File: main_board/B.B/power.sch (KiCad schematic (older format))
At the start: 36 parts, among them Q1 CJ3134K, Q2 CJ3134K, U62 AOZ1280, U63 FP6296

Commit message: nabijecka
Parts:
- removed C100: 47nf, Capacitor_SMD:C_0603_1608Metric, symbol Device:C
- removed C101: 10pf, Capacitor_SMD:C_0402_1005Metric, symbol Device:C
- removed C91, C95: 22uf, Capacitor_SMD:C_0805_2012Metric, symbol Device:C
- removed C96: 2.2uf, Capacitor_SMD:C_0805_2012Metric, symbol Device:C
- removed C97: 100nf, Capacitor_SMD:C_0402_1005Metric, symbol Device:C
- removed C98: 1nf, Capacitor_SMD:C_0402_1005Metric, symbol Device:C
- removed C99: 1uf, Capacitor_SMD:C_0402_1005Metric, symbol Device:C
- removed D2: SS54, BB:DO-214AC, symbol Device:D_Schottky
- removed L2: 3.3uH, BB:SMD-PIND-12.8x13.5x5_2.0x5.0, symbol Device:L
- removed Q2: CJ3134K, Package_TO_SOT_SMD:SOT-23, symbol Transistor_FET:2N7002
- removed R13: 10, Resistor_SMD:R_0402_1005Metric, symbol Device:R
- removed R15: 1.5, Resistor_SMD:R_0402_1005Metric, symbol Device:R
- removed R16: 24k, Resistor_SMD:R_0402_1005Metric, symbol Device:R
- removed R17: 100k, Resistor_SMD:R_0402_1005Metric, symbol Device:R
- removed R19: 8,2k, Resistor_SMD:R_0402_1005Metric, symbol Device:R
- removed U63: FP6296, BB:SOP-8+1_3.76x4.96mm_P1.27mm, symbol B.B-rescue:FP6296
- added C61: 1uf, Capacitor_SMD:C_0402_1005Metric, symbol Device:C
- added C62: 2.2uf, Capacitor_SMD:C_0805_2012Metric, symbol Device:C
- added C?: 22uf, Capacitor_SMD:C_0805_2012Metric, symbol Device:C
- added L?: 2.2uH, BB:MWSA0603_6.6x7.1x3.0, symbol Device:L
- added Q?: 2N7002, Package_TO_SOT_SMD:SOT-23, symbol Transistor_FET:2N7002
- added R7, R8: 1M, Resistor_SMD:R_0402_1005Metric, symbol Device:R
- added R?: 7.5k, Resistor_SMD:R_0402_1005Metric, symbol Device:R
- added R?: 56k, Resistor_SMD:R_0402_1005Metric, symbol Device:R
- added SW3: SW_DIP_x01, Button_Switch_SMD:SW_Push_1P1T_NO_CK_KSC6xxJ, symbol Switch:SW_DIP_x01
- added U?: FP6276, Package_SO:SOP-8_3.76x4.96mm_P1.27mm, symbol B.B-rescue:FP6276
- L1: footprint BB:SMD-PIND-10.5x11.5x4_2.5x3.0 -> BB:MWSA0603_6.6x7.1x3.0; LCSC C149550 -> C112126
- Q1: value CJ3134K -> 2N7002; LCSC C110100 -> C8545
- R14: value 75k -> 56k; LCSC C25798 -> C25796
- gave numbers to parts that had none: 2
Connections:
- wire segments 77 -> 71

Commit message: 18650
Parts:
- removed C86: 2.2uf, Capacitor_SMD:C_0805_2012Metric, symbol Device:C
- gave numbers to parts that had none: 6
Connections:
- wire segments 71 -> 69

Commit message: polifuse
-filtr k prijmaci IR
-merwni bterky -> za zapinani
-odstraneni odpojovani nabijecky + oprava napajeciho prouhu
-odstraneni prevodniku napeti k WS2812
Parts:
- added R3: 1M, Resistor_SMD:R_0402_1005Metric, symbol Device:R
- added R4: 300k, Capacitor_SMD:C_0402_1005Metric, symbol Device:R
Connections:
- net labels added: VCC-OUT, baterimetr
- wire segments 69 -> 74
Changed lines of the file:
@@
 Connection ~ 4950 2525
 Connection ~ 4625 2525
+$Comp
+L Device:R R?
+U 1 1 5FBC25E2
+P 3975 4750
+AR Path="/5FBC25E2" Ref="R?"  Part="1"
+AR Path="/5FA4C94D/5FBC25E2" Ref="R4"  Part="1"
+F 0 "R4" H 4045 4796 50  0000 L CNN
+F 1 "300k" H 4045 4705 50  0000 L CNN
+F 2 "Capacitor_SMD:C_0402_1005Metric" V 3905 4750 50  0001 C CNN
+F 3 "~" H 3975 4750 50  0001 C CNN
+F 4 "C25774" H 3975 4750 50  0001 C CNN "LCSC"
+	1    3975 4750
+	1    0    0    -1
+$EndComp
+$Comp
+L B.B-eagle-import:GND #GND?
+U 1 1 5FBC25E8
+P 3975 5000
+AR Path="/5FBC25E8" Ref="#GND?"  Part="1"
+AR Path="/5FA4C94D/5FBC25E8" Ref="#GND0158"  Part="1"
+F 0 "#GND0158" H 3975 5000 50  0001 C CNN
+F 1 "GND" H 3975 4920 59  0000 C CNN
+F 2 "" H 3975 5000 50  0001 C CNN
+F 3 "" H 3975 5000 50  0001 C CNN
+	1    3975 5000
+	1    0    0    -1
+$EndComp
+Wire Wire Line
+	3825 4600 3975 4600
+$Comp
+L Device:R R?
+U 1 1 5FBC25F0
+P 3975 4450
+AR Path="/5F77B818/5FBC25F0" Ref="R?"  Part="1"
+AR Path="/5FBC25F0" Ref="R?"  Part="1"
+AR Path="/5FA4C94D/5FBC25F0" Ref="R3"  Part="1"
+F 0 "R3" H 4045 4496 50  0000 L CNN
+F 1 "1M" H 4045 4405 50  0000 L CNN
+F 2 "Resistor_SMD:R_0402_1005Metric" V 3905 4450 50  0001 C CNN
+F 3 "~" H 3975 4450 50  0001 C CNN
+F 4 "C26083" H 3975 4450 50  0001 C CNN "LCSC"
+	1    3975 4450
+	1    0    0    -1
+$EndComp
+Connection ~ 3975 4600
+Wire Wire Line
+	3975 4300 3975 4275
+Wire Wire Line
+	3975 4275 4625 4275
+Text HLabel 3825 4600 0    50   Input ~ 0
+baterimetr
+Text HLabel 4675 2425 2    50   Input ~ 0
+VCC-OUT
+Wire Wire Line
+	4675 2425 4625 2425
+Wire Wire Line
+	4625 2425 4625 2525
 $EndSCHEMATC

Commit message: popisky
-popisky
-poladeni uddeleni enkoderu
-poladeni nayvu drah
-priopjeni gnd USB
-poligon V5 na led-desce do spodni vrstvu
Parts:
- C61, C62, C75, C85, C87, C88, C89, C90, C92, C93: symbol Device:C -> B.B-rescue:C-Device
- D1: symbol Device:D_Schottky -> B.B-rescue:D_Schottky-Device
- L1, L2: symbol Device:L -> B.B-rescue:L-Device
- Q1, Q2: symbol Transistor_FET:2N7002 -> B.B-rescue:2N7002-Transistor_FET
- R10, R11, R12, R13, R14, R15, R18, R3, R4, R6, R7, R8: symbol Device:R -> B.B-rescue:R-Device
- SW3: symbol Switch:SW_DIP_x01 -> B.B-rescue:SW_DIP_x01-Switch
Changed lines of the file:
@@
 EESchema Schematic File Version 4
-LIBS:B.B-cache
-EELAYER 29 0
+EELAYER 30 0
 EELAYER END
 $Descr A4 11693 8268
@@
 $EndComp
 $Comp
-L Device:C C88
+L B.B-rescue:C-Device C88
 U 1 1 5FA5C393
 P 7725 2825
@@
 $EndComp
 $Comp
-L Device:C C87
+L B.B-rescue:C-Device C87
 U 1 1 5FA66714
 P 4950 2725
@@
 $EndComp
 $Comp
-L Device:R R10
+L B.B-rescue:R-Device R10
 U 1 1 5FA82308
 P 5575 2675
@@
 	5275 2525 5925 2525
 $Comp
-L Device:R R11
+L B.B-rescue:R-Device R11
 U 1 1 5FAAA54F
 P 6925 2725
@@
 	7225 2775 7225 2625
 $Comp
-L Device:R R12
+L B.B-rescue:R-Device R12
 U 1 1 5FAAA559
 P 6625 2925
@@
 	7225 2625 7275 2625
 $Comp
-L Device:C C85
+L B.B-rescue:C-Device C85
 U 1 1 5FACBCDA
 P 6775 2525
@@
 	7225 2525 7225 2625
 $Comp
-L Device:D_Schottky D1
+L B.B-rescue:D_Schottky-Device D1
 U 1 1 5FAEBDB1
 P 7225 2925
@@
 Connection ~ 7625 2625
 $Comp
-L Device:R R14
+L B.B-rescue:R-Device R14
 U 1 1 5FA6804A
 P 6775 4475
@@
 $EndComp
 $Comp
-L Device:C C92
+L B.B-rescue:C-Device C92
 U 1 1 5FA68060
 P 7125 4475
@@
 $EndComp
 $Comp
-L Device:C C93
+L B.B-rescue:C-Device C93
 U 1 1 5FA68067
 P 7550 4475
@@
 $EndComp
 $Comp
-L Device:C C90
+L B.B-rescue:C-Device C90
 U 1 1 5FCAA96B
 P 4625 4475
@@
 	5625 4275 5475 4275
 $Comp
-L Transistor_FET:2N7002 Q?
+L B.B-rescue:2N7002-Transistor_FET Q?
 U 1 1 5FA8B0DC
 P 3275 3025
@@
 $EndComp
 $Comp
-L Device:R R6
+L B.B-rescue:R-Device R6
 U 1 1 602F171D
 P 3175 2825
@@
 pull-up to 3V3 in ESP32
 $Comp
-L Device:L L1
+L B.B-rescue:L-Device L1
 U 1 1 5FBDFC00
 P 7425 2625
@@
 SHUTDOWN_3V3-5V
 $Comp
-L Device:C C62
+L B.B-rescue:C-Device C62
 U 1 1 5FC4D1AC
 P 2925 3225
@@
 $EndComp
 $Comp
-L Device:R R?
+L B.B-rescue:R-Device R?
 U 1 1 5FC4F9B1
 P 2625 3225
@@
 	2625 3075 2625 3025
 $Comp
-L Switch:SW_DIP_x01 SW?
+L B.B-rescue:SW_DIP_x01-Switch SW?
 U 1 1 5FC5B229
 P 4275 3500
@@
 $EndComp
 $Comp
-L Device:C C61
+L B.B-rescue:C-Device C61
 U 1 1 5FC601F5
 P 4050 2825
@@
 $EndComp
 $Comp
-L Device:R R?
+L B.B-rescue:R-Device R?
 U 1 1 5FC61828
 P 4050 3050
@@
 	5550 4800 5550 4675
 $Comp
-L Transistor_FET:2N7002 Q?
+L B.B-rescue:2N7002-Transistor_FET Q?
 U 1 1 5FBA36C7
 P 5450 5000
@@
 $EndComp
 $Comp
-L Device:R R18
+L B.B-rescue:R-Device R18
 U 1 1 5FCDFEDA
 P 5325 4675
@@
 	7550 4275 7975 4275
 $Comp
-L Device:R R13
+L B.B-rescue:R-Device R13
 U 1 1 5FBBDF29
 P 6775 4775
@@
 Connection ~ 6775 4625
 $Comp
-L Device:C C75
+L B.B-rescue:C-Device C75
 U 1 1 5FBDCDD3
 P 7975 4475
@@
 	7975 4275 8325 4275
 $Comp
-L Device:L L2
+L B.B-rescue:L-Device L2
 U 1 1 5FBEEA97
 P 5325 4275
@@
 $EndComp
 $Comp
-L Device:R R15
+L B.B-rescue:R-Device R15
 U 1 1 5FBF0991
 P 6375 4875
@@
 $EndComp
 $Comp
-L Device:C C89
+L B.B-rescue:C-Device C89
 U 1 1 5FA5C39A
 P 8125 2825
@@
 Connection ~ 4625 2525
 $Comp
-L Device:R R?
+L B.B-rescue:R-Device R?
 U 1 1 5FBC25E2
 P 3975 4750
@@
 	3825 4600 3975 4600
 $Comp
-L Device:R R?
+L B.B-rescue:R-Device R?
 U 1 1 5FBC25F0
 P 3975 4450

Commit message: LDC footprint
prodlouzeni pedu pro usnadneni rucniho osazovani
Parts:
- C61, C62, C75, C85, C87, C88, C89, C90, C92, C93: symbol B.B-rescue:C-Device -> B.B-rescue:C-Device-B.B-rescue
- D1: symbol B.B-rescue:D_Schottky-Device -> B.B-rescue:D_Schottky-Device-B.B-rescue
- L1, L2: symbol B.B-rescue:L-Device -> B.B-rescue:L-Device-B.B-rescue
- Q1, Q2: symbol B.B-rescue:2N7002-Transistor_FET -> B.B-rescue:2N7002-Transistor_FET-B.B-rescue
- Q5: symbol B.B-rescue:Q_PMOS_DSG -> B.B-rescue:Q_PMOS_DSG-B.B-rescue
- R10, R11, R12, R13, R14, R15, R18, R3, R4, R6, R7, R8: symbol B.B-rescue:R-Device -> B.B-rescue:R-Device-B.B-rescue
- SW3: symbol B.B-rescue:SW_DIP_x01-Switch -> B.B-rescue:SW_DIP_x01-Switch-B.B-rescue
- U62: symbol B.B-rescue:AOZ1280 -> B.B-rescue:AOZ1280-B.B-rescue
- U63: symbol B.B-rescue:FP6276 -> B.B-rescue:FP6276-B.B-rescue
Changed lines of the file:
@@
 VCC
 $Comp
-L B.B-rescue:AOZ1280 U62
+L B.B-rescue:AOZ1280-B.B-rescue U62
 U 1 1 5FA53B6D
 P 6225 2525
@@
 $EndComp
 $Comp
-L B.B-rescue:C-Device C88
+L B.B-rescue:C-Device-B.B-rescue C88
 U 1 1 5FA5C393
 P 7725 2825
@@
 	7725 2675 7725 2625
 $Comp
-L B.B-eagle-import:GND #GND088
+L B.B-rescue:GND-B.B-eagle-import #GND088
 U 1 1 5FA5C3A3
 P 7725 3075
@@
 $EndComp
 $Comp
-L B.B-rescue:C-Device C87
+L B.B-rescue:C-Device-B.B-rescue C87
 U 1 1 5FA66714
 P 4950 2725
@@
 $EndComp
 $Comp
-L B.B-eagle-import:GND #GND086
+L B.B-rescue:GND-B.B-eagle-import #GND086
 U 1 1 5FA6671A
 P 4950 2975
@@
 	6525 2625 7225 2625
 $Comp
-L B.B-eagle-import:GND #GND087
+L B.B-rescue:GND-B.B-eagle-import #GND087
 U 1 1 5FA8018B
 P 6225 2975
@@
 $EndComp
 $Comp
-L B.B-rescue:R-Device R10
+L B.B-rescue:R-Device-B.B-rescue R10
 U 1 1 5FA82308
 P 5575 2675
@@
 	5275 2675 5275 2525
 $Comp
-L B.B-eagle-import:GND #GND?
+L B.B-rescue:GND-B.B-eagle-import #GND?
 U 1 1 5FA8231A
 P 3375 3325
@@
 	5275 2525 5925 2525
 $Comp
-L B.B-rescue:R-Device R11
+L B.B-rescue:R-Device-B.B-rescue R11
 U 1 1 5FAAA54F
 P 6925 2725
@@
 	7225 2775 7225 2625
 $Comp
-L B.B-rescue:R-Device R12
+L B.B-rescue:R-Device-B.B-rescue R12
 U 1 1 5FAAA559
 P 6625 2925
@@
 	6625 2725 6525 2725
 $Comp
-L B.B-eagle-import:GND #GND090
+L B.B-rescue:GND-B.B-eagle-import #GND090
 U 1 1 5FAAA562
 P 6625 3175
@@
 	7225 2625 7275 2625
 $Comp
-L B.B-rescue:C-Device C85
+L B.B-rescue:C-Device-B.B-rescue C85
 U 1 1 5FACBCDA
 P 6775 2525
@@
 	7225 2525 7225 2625
 $Comp
-L B.B-rescue:D_Schottky-Device D1
+L B.B-rescue:D_Schottky-Device-B.B-rescue D1
 U 1 1 5FAEBDB1
 P 7225 2925
@@
 $EndComp
 $Comp
-L B.B-eagle-import:GND #GND091
+L B.B-rescue:GND-B.B-eagle-import #GND091
 U 1 1 5FAECA44
 P 7225 3175
@@
 Connection ~ 7625 2625
 $Comp
-L B.B-rescue:R-Device R14
+L B.B-rescue:R-Device-B.B-rescue R14
 U 1 1 5FA6804A
 P 6775 4475
@@
 $EndComp
 $Comp
-L B.B-eagle-import:GND #GND0102
+L B.B-rescue:GND-B.B-eagle-import #GND0102
 U 1 1 5FA68059
 P 6775 5025
@@
 $EndComp
 $Comp
-L B.B-rescue:C-Device C92
+L B.B-rescue:C-Device-B.B-rescue C92
 U 1 1 5FA68060
 P 7125 4475
@@
 $EndComp
 $Comp
-L B.B-rescue:C-Device C93
+L B.B-rescue:C-Device-B.B-rescue C93
 U 1 1 5FA68067
 P 7550 4475
@@
 	7125 4275 7550 4275
 $Comp
-L B.B-eagle-import:GND #GND096
+L B.B-rescue:GND-B.B-eagle-import #GND096
 U 1 1 5FA68099
 P 7125 4725
@@
 $EndComp
 $Comp
-L B.B-eagle-import:GND #GND097
+L B.B-rescue:GND-B.B-eagle-import #GND097
 U 1 1 5FA6809F
 P 7550 4725
@@
 	6775 4275 7125 4275
 $Comp
-L B.B-eagle-import:GND #GND0106
+L B.B-rescue:GND-B.B-eagle-import #GND0106
 U 1 1 5FBAAAC6
 P 5975 4925
@@
 $EndComp
 $Comp
-L B.B-rescue:C-Device C90
+L B.B-rescue:C-Device-B.B-rescue C90
 U 1 1 5FCAA96B
 P 4625 4475
@@
 	4625 4325 4625 4275
 $Comp
-L B.B-eagle-import:GND #GND094
+L B.B-rescue:GND-B.B-eagle-import #GND094
 U 1 1 5FCAA97A
 P 4625 4725
@@
 	5625 4275 5475 4275
 $Comp
-L B.B-rescue:2N7002-Transistor_FET Q?
+L B.B-rescue:2N7002-Transistor_FET-B.B-rescue Q?
 U 1 1 5FA8B0DC
 P 3275 3025
@@
 	5725 2675 5925 2675
 $Comp
-L B.B-rescue:Q_PMOS_DSG Q?
+L B.B-rescue:Q_PMOS_DSG-B.B-rescue Q?
 U 1 1 602B4407
 P 3375 2625
@@
 $EndComp
 $Comp
-L B.B-rescue:R-Device R6
+L B.B-rescue:R-Device-B.B-rescue R6
 U 1 1 602F171D
 P 3175 2825
@@
 pull-up to 3V3 in ESP32
 $Comp
-L B.B-rescue:L-Device L1
+L B.B-rescue:L-Device-B.B-rescue L1
 U 1 1 5FBDFC00
 P 7425 2625
@@
 SHUTDOWN_3V3-5V
 $Comp
-L B.B-rescue:C-Device C62
+L B.B-rescue:C-Device-B.B-rescue C62
 U 1 1 5FC4D1AC
 P 2925 3225
@@
 	2925 3025 2925 3075
 $Comp
-L B.B-eagle-import:GND #GND0131
+L B.B-rescue:GND-B.B-eagle-import #GND0131
 U 1 1 5FC4D1B3
 P 2925 3475
@@
 $EndComp
 $Comp
-L B.B-rescue:R-Device R?
+L B.B-rescue:R-Device-B.B-rescue R?
 U 1 1 5FC4F9B1
 P 2625 3225
@@
 $EndComp
 $Comp
-L B.B-eagle-import:GND #GND0135
+L B.B-rescue:GND-B.B-eagle-import #GND0135
 U 1 1 5FC515F0
 P 2625 3475
@@
 	2625 3075 2625 3025
 $Comp
-L B.B-rescue:SW_DIP_x01-Switch SW?
+L B.B-rescue:SW_DIP_x01-Switch-B.B-rescue SW?
 U 1 1 5FC5B229
 P 4275 3500
@@
 $EndComp
 $Comp
-L B.B-rescue:C-Device C61
+L B.B-rescue:C-Device-B.B-rescue C61
 U 1 1 5FC601F5
 P 4050 2825
@@
 $EndComp
 $Comp
-L B.B-rescue:R-Device R?
+L B.B-rescue:R-Device-B.B-rescue R?
 U 1 1 5FC61828
 P 4050 3050
@@
 	4275 3050 4275 3200
 $Comp
-L B.B-eagle-import:GND #GND0136
+L B.B-rescue:GND-B.B-eagle-import #GND0136
 U 1 1 5FC7161E
 P 4275 3900
@@
 $EndComp
 $Comp
-L B.B-rescue:FP6276 U63
+L B.B-rescue:FP6276-B.B-rescue U63
 U 1 1 5FB47E0B
 P 5975 4275
@@
 	6375 4675 6325 4675
 $Comp
-L B.B-eagle-import:GND #GND0101
+L B.B-rescue:GND-B.B-eagle-import #GND0101
 U 1 1 5FB82735
 P 6375 5125
@@
 	5550 4800 5550 4675
 $Comp
-L B.B-rescue:2N7002-Transistor_FET Q?
+L B.B-rescue:2N7002-Transistor_FET-B.B-rescue Q?
 U 1 1 5FBA36C7
 P 5450 5000
@@
 	5550 4675 5625 4675
 $Comp
-L B.B-eagle-import:GND #GND?
+L B.B-rescue:GND-B.B-eagle-import #GND?
 U 1 1 5FCDFEEC
 P 5550 5300
@@
 $EndComp
 $Comp
-L B.B-rescue:R-Device R18
+L B.B-rescue:R-Device-B.B-rescue R18
 U 1 1 5FCDFEDA
 P 5325 4675
@@
 	7550 4275 7975 4275
 $Comp
-L B.B-rescue:R-Device R13
+L B.B-rescue:R-Device-B.B-rescue R13
 U 1 1 5FBBDF29
 P 6775 4775
@@
 Connection ~ 6775 4625
 $Comp
-L B.B-rescue:C-Device C75
+L B.B-rescue:C-Device-B.B-rescue C75
 U 1 1 5FBDCDD3
 P 7975 4475
@@
 	7975 4325 7975 4275
 $Comp
-L B.B-eagle-import:GND #GND0103
+L B.B-rescue:GND-B.B-eagle-import #GND0103
 U 1 1 5FBDCDDA
 P 7975 4725
@@
 	7975 4275 8325 4275
 $Comp
-L B.B-rescue:L-Device L2
+L B.B-rescue:L-Device-B.B-rescue L2
 U 1 1 5FBEEA97
 P 5325 4275
@@
 $EndComp
 $Comp
-L B.B-rescue:R-Device R15
+L B.B-rescue:R-Device-B.B-rescue R15
 U 1 1 5FBF0991
 P 6375 4875
@@
 	8125 2625 8125 2675
 $Comp
-L B.B-eagle-import:GND #GND089
+L B.B-rescue:GND-B.B-eagle-import #GND089
 U 1 1 5FA5C3AF
 P 8125 3075
@@
 $EndComp
 $Comp
-L B.B-rescue:C-Device C89
+L B.B-rescue:C-Device-B.B-rescue C89
 U 1 1 5FA5C39A
 P 8125 2825
@@
 Connection ~ 4625 2525
 $Comp
-L B.B-rescue:R-Device R?
+L B.B-rescue:R-Device-B.B-rescue R?
 U 1 1 5FBC25E2
 P 3975 4750
@@
 $EndComp
 $Comp
-L B.B-eagle-import:GND #GND?
+L B.B-rescue:GND-B.B-eagle-import #GND?
 U 1 1 5FBC25E8
 P 3975 5000
@@
 	3825 4600 3975 4600
 $Comp
-L B.B-rescue:R-Device R?
+L B.B-rescue:R-Device-B.B-rescue R?
 U 1 1 5FBC25F0
 P 3975 4450

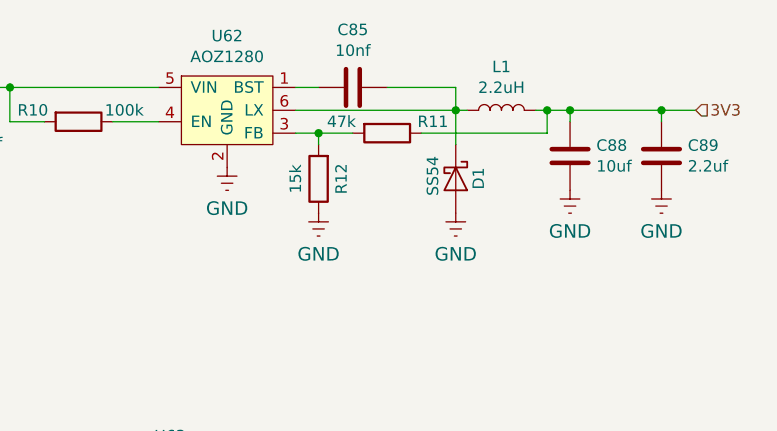
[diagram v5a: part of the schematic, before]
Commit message: JLCdata
- korekce pozice a natoceni
- data pro vyrobu
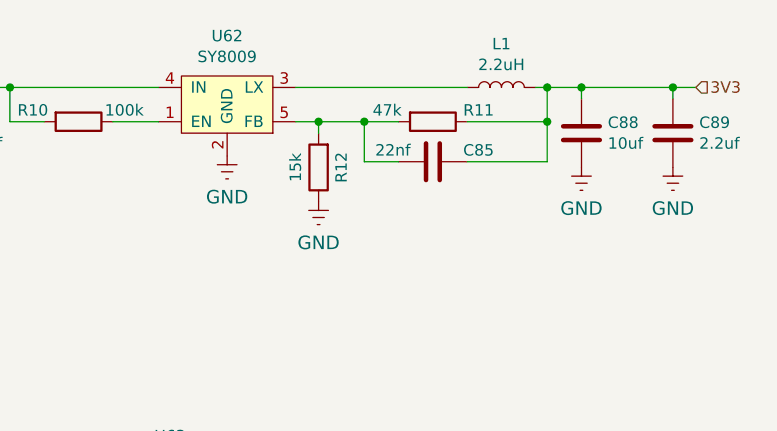
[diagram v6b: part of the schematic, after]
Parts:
- removed D1: SS54, BB:DO-214AC, symbol B.B-rescue:D_Schottky-Device-B.B-rescue
- removed U62: AOZ1280, Package_TO_SOT_SMD:SOT-23-6, symbol B.B-rescue:AOZ1280-B.B-rescue
- added U62: SY8009, Package_TO_SOT_SMD:SOT-23-5, symbol B.B-rescue:SY8009
- C85: value 10nf -> 22nf; LCSC C15195 -> C1555
- L1, L2: LCSC C112126 -> C351096
- Q1, Q2: JLCPCB_CORRECTION (none) -> 0;0;180
- Q5: LCSC C145421 -> C144884
- U63: JLCPCB_CORRECTION (none) -> 0;0;-90
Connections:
- net 3V3: now also C85.1
- net VCC-OUT: now also U62.4 (IN)
- net at C85.2: now also R11.2, R12.2, U62.5 (FB)
- net at R10.1: now also U62.1 (EN)
- net at L1.1: now also U62.3 (LX); no longer C85.1
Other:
- moved on the sheet: C85, C88, C89, L1, R11, R12

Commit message: opravi_a_dodatky MPU/QMC/conn_A9G
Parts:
- removed C85: 22nf, Capacitor_SMD:C_0402_1005Metric, symbol B.B-rescue:C-Device-B.B-rescue
- removed L1: 2.2uH, BB:MWSA0603_6.6x7.1x3.0, symbol B.B-rescue:L-Device-B.B-rescue
- removed R11: 47k, Resistor_SMD:R_0402_1005Metric, symbol B.B-rescue:R-Device-B.B-rescue
- removed R12: 15k, Resistor_SMD:R_0402_1005Metric, symbol B.B-rescue:R-Device-B.B-rescue
- removed U62: SY8009, Package_TO_SOT_SMD:SOT-23-5, symbol B.B-rescue:SY8009
- added SW5: SW_DIP_x01, Button_Switch_SMD:SW_Push_1P1T_NO_CK_KSC6xxJ, symbol B.B-rescue:SW_DIP_x01-Switch-B.B-rescue
- added U62: NCP708, Package_DFN_QFN:DFN-6-1EP_3x3mm_P0.95mm_EP1.7x2.6mm, symbol B.B-rescue:NCP708
- U63: footprint Package_SO:SOP-8_3.76x4.96mm_P1.27mm -> Package_SO:SOIC-8-1EP_3.9x4.9mm_P1.27mm_EP2.41x3.81mm_ThermalVias
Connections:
- net 3V3: now also U62.4 (Vout), U62.5 (SNS)
- net SHUTDOWN_3V3-5V: now also SW5.2
- net VCC-OUT: now also U62.6 (Vin)
- net at R10.1: now also U62.1 (EN)
- new net GND: U62.2 (GND), U62.7 (GND)
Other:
- moved on the sheet: C88, C89, R10

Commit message: opravy_a_dodatky_2
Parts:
- removed SW5: SW_DIP_x01, Button_Switch_SMD:SW_Push_1P1T_NO_CK_KSC6xxJ, symbol B.B-rescue:SW_DIP_x01-Switch-B.B-rescue
- removed U62: NCP708, Package_DFN_QFN:DFN-6-1EP_3x3mm_P0.95mm_EP1.7x2.6mm, symbol B.B-rescue:NCP708
- added C85: 22nf, Capacitor_SMD:C_0402_1005Metric, symbol B.B-rescue:C-Device-B.B-rescue
- added L1: 2.2uH, BB:MWSA0603_6.6x7.1x3.0, symbol B.B-rescue:L-Device-B.B-rescue
- added R11: 47k, Resistor_SMD:R_0402_1005Metric, symbol B.B-rescue:R-Device-B.B-rescue
- added R12: 15k, Resistor_SMD:R_0402_1005Metric, symbol B.B-rescue:R-Device-B.B-rescue
- added U62: SY8009, Package_TO_SOT_SMD:SOT-23-5, symbol B.B-rescue:SY8009
- U63: footprint Package_SO:SOIC-8-1EP_3.9x4.9mm_P1.27mm_EP2.41x3.81mm_ThermalVias -> Package_SO:SOP-8_3.76x4.96mm_P1.27mm
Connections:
- net 3V3: now also C85.1, L1.2, R11.1
- net VCC-OUT: now also U62.4 (IN)
- net at R10.1: now also U62.1 (EN)
- new net: C85.2, R11.2, R12.2, U62.5 (FB)
- new net: L1.1, U62.3 (LX)
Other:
- moved on the sheet: C88, C89, R10
